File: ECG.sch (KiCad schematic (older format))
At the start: 16 parts, among them P1 MountingHole_Pad, P2 MountingHole_Pad, P3 MountingHole_Pad, U1 ADR4525, U2 SP6641

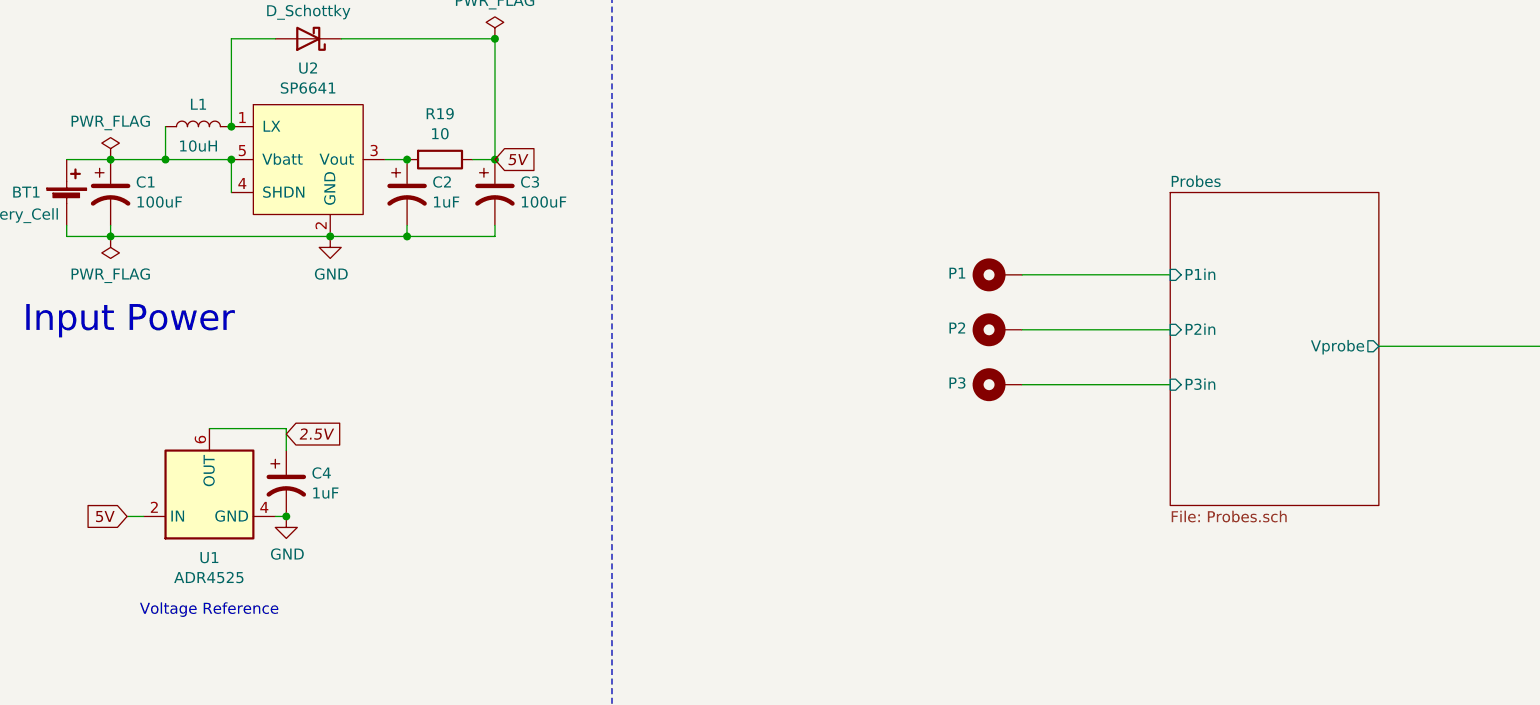
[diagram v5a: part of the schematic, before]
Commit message: #2 - Add ECG input via headphone jack
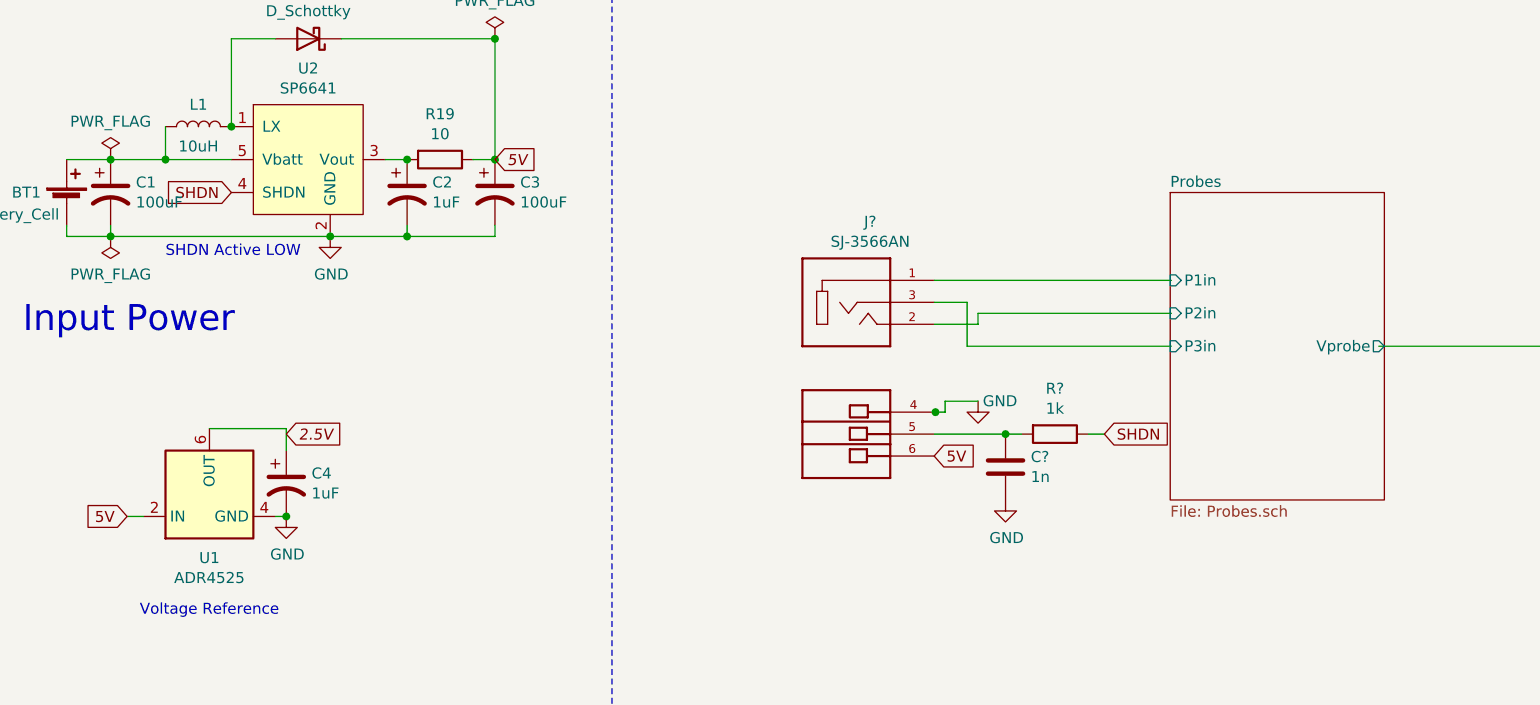
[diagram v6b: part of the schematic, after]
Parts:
- removed P1, P2, P3: MountingHole_Pad, MountingHole:MountingHole_6mm_Pad_Via, symbol Mechanical:MountingHole_Pad
- added C?: 1n, Capacitor_SMD:C_0805_2012Metric_Pad1.18x1.45mm_HandSolder, symbol Device:C
- added J?: SJ-3566AN, CUI_SJ-3566AN, symbol Audio_Connectors:SJ-3566AN
- added R?: 1k, Resistor_SMD:R_0805_2012Metric_Pad1.20x1.40mm_HandSolder, symbol Device:R
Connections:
- net labels added: SHDN
- wire segments 28 -> 38
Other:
- note added: "SHDN Active LOW\n"
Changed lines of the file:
@@
 Connection ~ 2400 4275
 $Sheet
-S 6425 2800 950  1425
+S 6425 2800 975  1400
 U 5F9F8A5A
 F0 "Probes" 50
 F1 "Probes.sch" 50
-F2 "Vprobe" O R 7375 3500 50
-F3 "P1in" I L 6425 3175 50
-F4 "P2in" I L 6425 3425 50
-F5 "P3in" I L 6425 3675 50
+F2 "Vprobe" O R 7400 3500 50
+F3 "P1in" I L 6425 3200 50
+F4 "P2in" I L 6425 3350 50
+F5 "P3in" I L 6425 3500 50
 $EndSheet
 $Sheet
@@
 Wire Wire Line
 	7375 3500 8375 3500
-$Comp
-L Mechanical:MountingHole_Pad P1
-U 1 1 5FA67DA7
-P 5650 3175
-F 0 "P1" V 5656 3327 50  0000 L CNN
-F 1 "MountingHole_Pad" V 5750 3133 50  0001 L CNN
-F 2 "MountingHole:MountingHole_6mm_Pad_Via" H 5650 3175 50  0001 C CNN
-F 3 "~" H 5650 3175 50  0001 C CNN
-	1    5650 3175
-	0    -1   -1   0
-$EndComp
-$Comp
-L Mechanical:MountingHole_Pad P2
-U 1 1 5FA685AE
-P 5650 3425
-F 0 "P2" V 5656 3577 50  0000 L CNN
-F 1 "MountingHole_Pad" V 5750 3383 50  0001 L CNN
-F 2 "MountingHole:MountingHole_6mm_Pad_Via" H 5650 3425 50  0001 C CNN
-F 3 "~" H 5650 3425 50  0001 C CNN
-	1    5650 3425
-	0    -1   -1   0
-$EndComp
-$Comp
-L Mechanical:MountingHole_Pad P3
-U 1 1 5FA686F5
-P 5650 3675
-F 0 "P3" V 5656 3827 50  0000 L CNN
-F 1 "MountingHole_Pad" V 5750 3633 50  0001 L CNN
-F 2 "MountingHole:MountingHole_6mm_Pad_Via" H 5650 3675 50  0001 C CNN
-F 3 "~" H 5650 3675 50  0001 C CNN
-	1    5650 3675
-	0    -1   -1   0
-$EndComp
-Wire Wire Line
-	5750 3175 6425 3175
-Wire Wire Line
-	5750 3425 6425 3425
-Wire Wire Line
-	6425 3675 5750 3675
 Wire Wire Line
 	10250 3500 9450 3500
@@
 $EndComp
 Wire Wire Line
-	2150 2650 2150 2800
-Connection ~ 2150 2650
-Wire Wire Line
 	1400 2650 1600 2650
 $Comp
@@
 $EndComp
 Connection ~ 3350 2100
+Text GLabel 2150 2800 0    50   Input ~ 0
+SHDN
+Text GLabel 6125 3900 2    50   Input ~ 0
+SHDN
+$Comp
+L Device:R R?
+U 1 1 5FBC4C0E
+P 5900 3900
+F 0 "R?" V 5693 3900 50  0000 C CNN
+F 1 "1k" V 5784 3900 50  0000 C CNN
+F 2 "Resistor_SMD:R_0805_2012Metric_Pad1.20x1.40mm_HandSolder" V 5830 3900 50  0001 C CNN
+F 3 "~" H 5900 3900 50  0001 C CNN
+	1    5900 3900
+	0    1    1    0
+$EndComp
+Wire Wire Line
+	6125 3900 6050 3900
+Text GLabel 5350 4000 2    50   Input ~ 0
+5V
+$Comp
+L power:GND #PWR?
+U 1 1 5FBD650D
+P 5550 3750
+F 0 "#PWR?" H 5550 3500 50  0001 C CNN
+F 1 "GND" H 5650 3750 50  0000 C CNN
+F 2 "" H 5550 3750 50  0001 C CNN
+F 3 "" H 5550 3750 50  0001 C CNN
+	1    5550 3750
+	1    0    0    -1
+$EndComp
+$Comp
+L power:GND #PWR?
+U 1 1 5FBD4F8F
+P 5675 4200
+F 0 "#PWR?" H 5675 3950 50  0001 C CNN
+F 1 "GND" H 5680 4027 50  0000 C CNN
+F 2 "" H 5675 4200 50  0001 C CNN
+F 3 "" H 5675 4200 50  0001 C CNN
+	1    5675 4200
+	1    0    0    -1
+$EndComp
+Connection ~ 5675 3900
+Wire Wire Line
+	5750 3900 5675 3900
+Wire Wire Line
+	5550 3350 6430 3350
+$Comp
+L Device:C C?
+U 1 1 5FBC41CD
+P 5675 4050
+F 0 "C?" H 5790 4096 50  0000 L CNN
+F 1 "1n" H 5790 4005 50  0000 L CNN
+F 2 "Capacitor_SMD:C_0805_2012Metric_Pad1.18x1.45mm_HandSolder" H 5713 3900 50  0001 C CNN
+F 3 "~" H 5675 4050 50  0001 C CNN
+	1    5675 4050
+	1    0    0    -1
+$EndComp
+$Comp
+L Audio_Connectors:SJ-3566AN J?
+U 1 1 5FBB1E3E
+P 4950 3300
+F 0 "J?" H 5059 3667 50  0000 C CNN
+F 1 "SJ-3566AN" H 5059 3576 50  0000 C CNN
+F 2 "CUI_SJ-3566AN" H 4950 3300 50  0001 L BNN
+F 3 "" H 4950 3300 50  0001 L BNN
+F 4 "Manufacturer recommendations" H 4950 3300 50  0001 L BNN "STANDARD"
+F 5 "" H 4950 3300 50  0001 L BNN "PARTREV"
+F 6 "CUI Inc" H 4950 3300 50  0001 L BNN "MF"
+	1    4950 3300
+	1    0    0    -1
+$EndComp
+Wire Wire Line
+	5550 3350 5550 3400
+Wire Wire Line
+	5500 3500 5500 3300
+Wire Wire Line
+	5500 3500 6430 3500
+Wire Wire Line
+	5400 3800 5400 3750
+Wire Wire Line
+	5400 3750 5550 3750
+Wire Wire Line
+	5350 3800 5356 3800
+Connection ~ 5356 3800
+Wire Wire Line
+	5356 3800 5400 3800
+Wire Wire Line
+	5350 3900 5675 3900
+Wire Wire Line
+	5350 3300 5500 3300
+Wire Wire Line
+	5350 3400 5550 3400
+Wire Wire Line
+	5350 3200 6430 3200
+Text Notes 1850 3100 0    50   ~ 0
+SHDN Active LOW\n
 $EndSCHEMATC

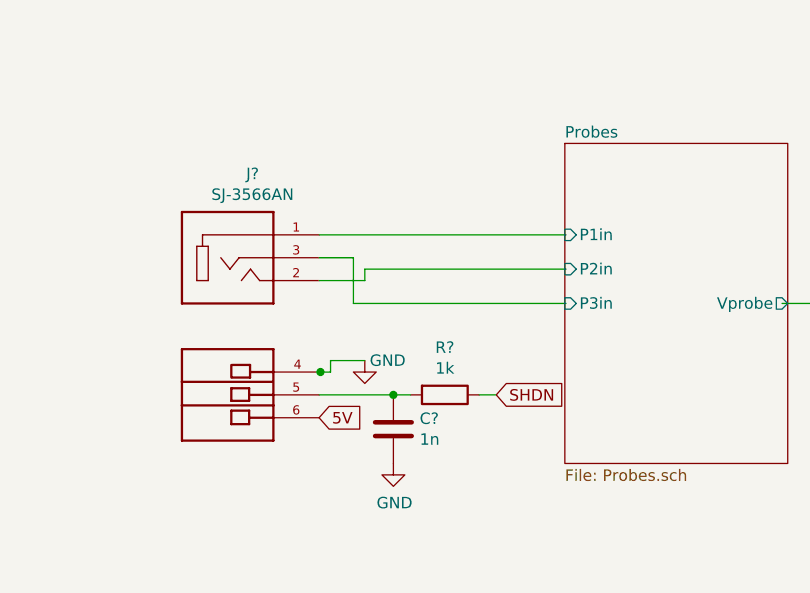
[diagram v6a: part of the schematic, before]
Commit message: #2 - Add ECG input via headphone jack
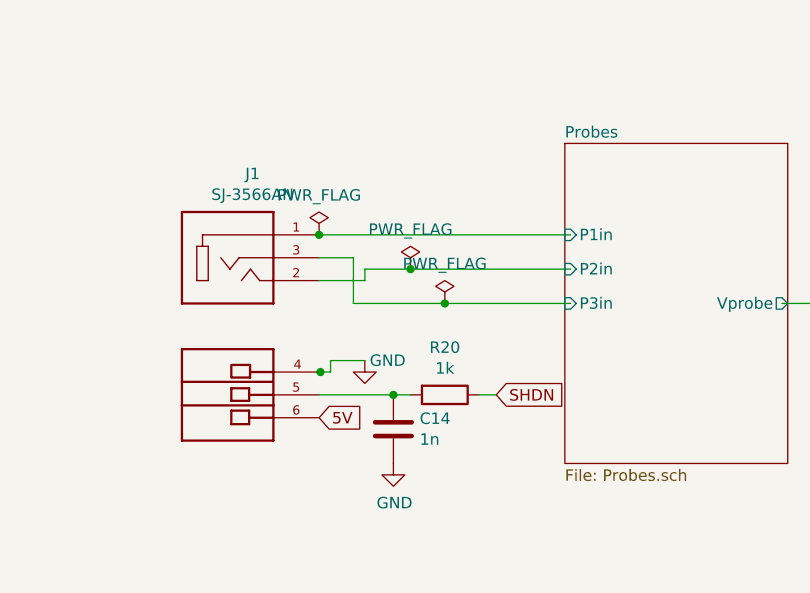
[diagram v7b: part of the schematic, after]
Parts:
- gave numbers to parts that had none: 3
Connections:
- wire segments 38 -> 40
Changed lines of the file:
@@
 SHDN
 $Comp
-L Device:R R?
+L Device:R R20
 U 1 1 5FBC4C0E
 P 5900 3900
-F 0 "R?" V 5693 3900 50  0000 C CNN
+F 0 "R20" V 5693 3900 50  0000 C CNN
 F 1 "1k" V 5784 3900 50  0000 C CNN
 F 2 "Resistor_SMD:R_0805_2012Metric_Pad1.20x1.40mm_HandSolder" V 5830 3900 50  0001 C CNN
@@
 5V
 $Comp
-L power:GND #PWR?
+L power:GND #PWR011
 U 1 1 5FBD650D
 P 5550 3750
-F 0 "#PWR?" H 5550 3500 50  0001 C CNN
+F 0 "#PWR011" H 5550 3500 50  0001 C CNN
 F 1 "GND" H 5650 3750 50  0000 C CNN
 F 2 "" H 5550 3750 50  0001 C CNN
@@
 $EndComp
 $Comp
-L power:GND #PWR?
+L power:GND #PWR012
 U 1 1 5FBD4F8F
 P 5675 4200
-F 0 "#PWR?" H 5675 3950 50  0001 C CNN
+F 0 "#PWR012" H 5675 3950 50  0001 C CNN
 F 1 "GND" H 5680 4027 50  0000 C CNN
 F 2 "" H 5675 4200 50  0001 C CNN
@@
 Wire Wire Line
 	5750 3900 5675 3900
-Wire Wire Line
-	5550 3350 6430 3350
 $Comp
-L Device:C C?
+L Device:C C14
 U 1 1 5FBC41CD
 P 5675 4050
-F 0 "C?" H 5790 4096 50  0000 L CNN
+F 0 "C14" H 5790 4096 50  0000 L CNN
 F 1 "1n" H 5790 4005 50  0000 L CNN
 F 2 "Capacitor_SMD:C_0805_2012Metric_Pad1.18x1.45mm_HandSolder" H 5713 3900 50  0001 C CNN
@@
 $EndComp
 $Comp
-L Audio_Connectors:SJ-3566AN J?
+L Audio_Connectors:SJ-3566AN J1
 U 1 1 5FBB1E3E
 P 4950 3300
-F 0 "J?" H 5059 3667 50  0000 C CNN
+F 0 "J1" H 5059 3667 50  0000 C CNN
 F 1 "SJ-3566AN" H 5059 3576 50  0000 C CNN
 F 2 "CUI_SJ-3566AN" H 4950 3300 50  0001 L BNN
@@
 Wire Wire Line
 	5500 3500 5500 3300
-Wire Wire Line
-	5500 3500 6430 3500
 Wire Wire Line
 	5400 3800 5400 3750
@@
 Wire Wire Line
 	5350 3400 5550 3400
-Wire Wire Line
-	5350 3200 6430 3200
 Text Notes 1850 3100 0    50   ~ 0
 SHDN Active LOW\n
+Wire Wire Line
+	5550 3350 5750 3350
+Wire Wire Line
+	5500 3500 5900 3500
+Wire Wire Line
+	6450 3200 5350 3200
+$Comp
+L power:PWR_FLAG #FLG0104
+U 1 1 5FBE011F
+P 5350 3200
+F 0 "#FLG0104" H 5350 3275 50  0001 C CNN
+F 1 "PWR_FLAG" H 5350 3373 50  0000 C CNN
+F 2 "" H 5350 3200 50  0001 C CNN
+F 3 "~" H 5350 3200 50  0001 C CNN
+	1    5350 3200
+	1    0    0    -1
+$EndComp
+Connection ~ 5350 3200
+$Comp
+L power:PWR_FLAG #FLG01
+U 1 1 5FBE0B2C
+P 5750 3350
+F 0 "#FLG01" H 5750 3425 50  0001 C CNN
+F 1 "PWR_FLAG" H 5750 3523 50  0000 C CNN
+F 2 "" H 5750 3350 50  0001 C CNN
+F 3 "~" H 5750 3350 50  0001 C CNN
+	1    5750 3350
+	1    0    0    -1
+$EndComp
+Connection ~ 5750 3350
+Wire Wire Line
+	5750 3350 6450 3350
+$Comp
+L power:PWR_FLAG #FLG02
+U 1 1 5FBE0E73
+P 5900 3500
+F 0 "#FLG02" H 5900 3575 50  0001 C CNN
+F 1 "PWR_FLAG" H 5900 3673 50  0000 C CNN
+F 2 "" H 5900 3500 50  0001 C CNN
+F 3 "~" H 5900 3500 50  0001 C CNN
+	1    5900 3500
+	1    0    0    -1
+$EndComp
+Connection ~ 5900 3500
+Wire Wire Line
+	5900 3500 6450 3500
 $EndSCHEMATC

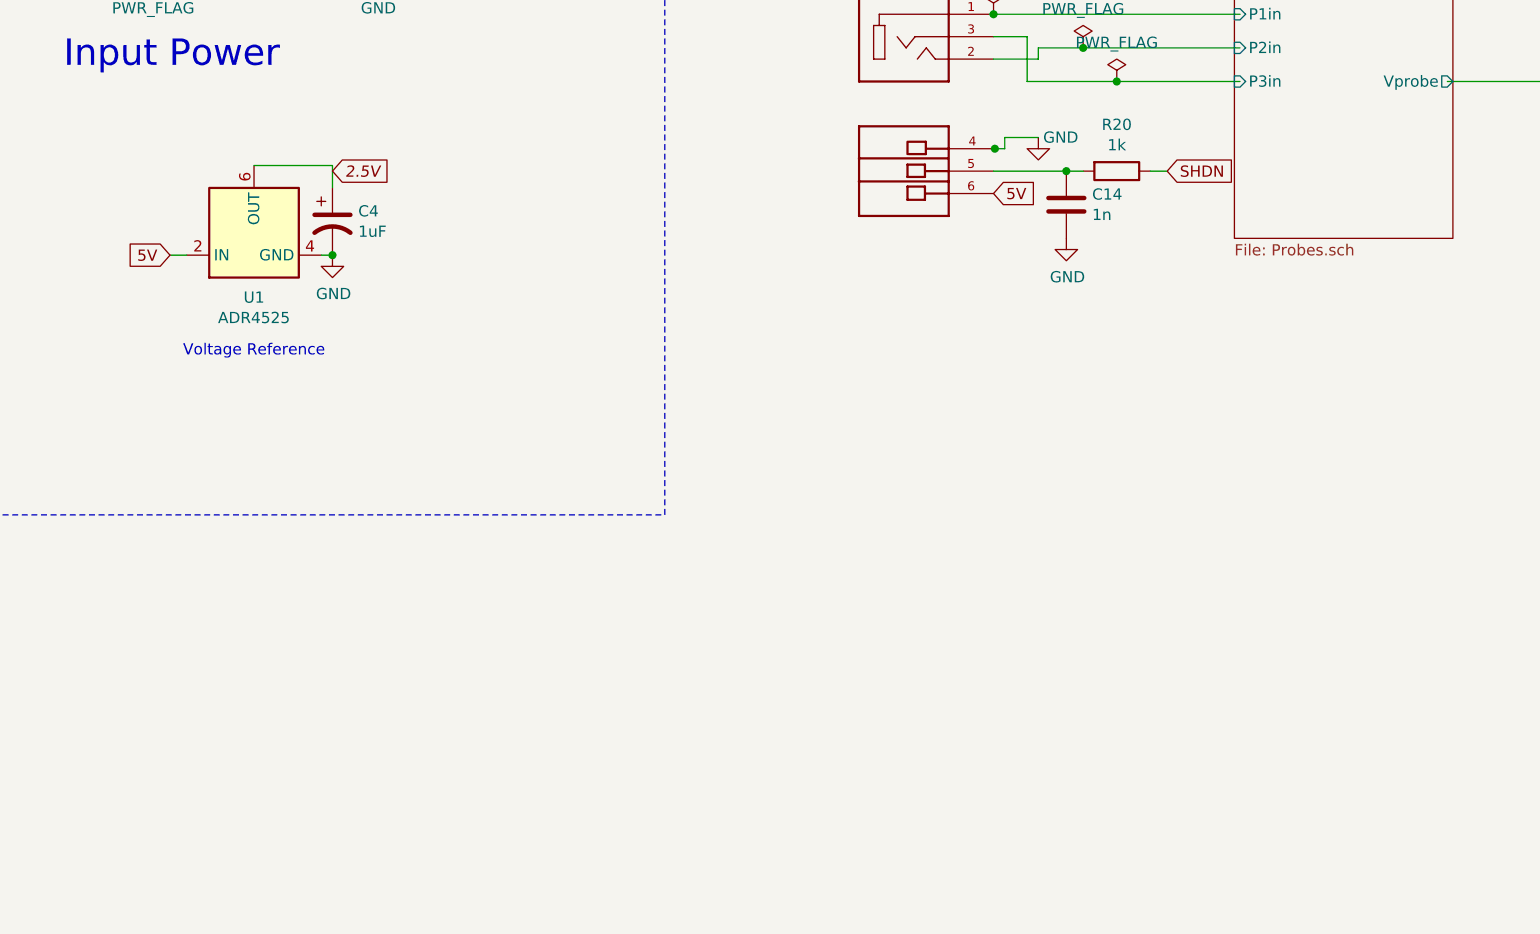
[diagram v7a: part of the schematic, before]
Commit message: #3 - Add power switch
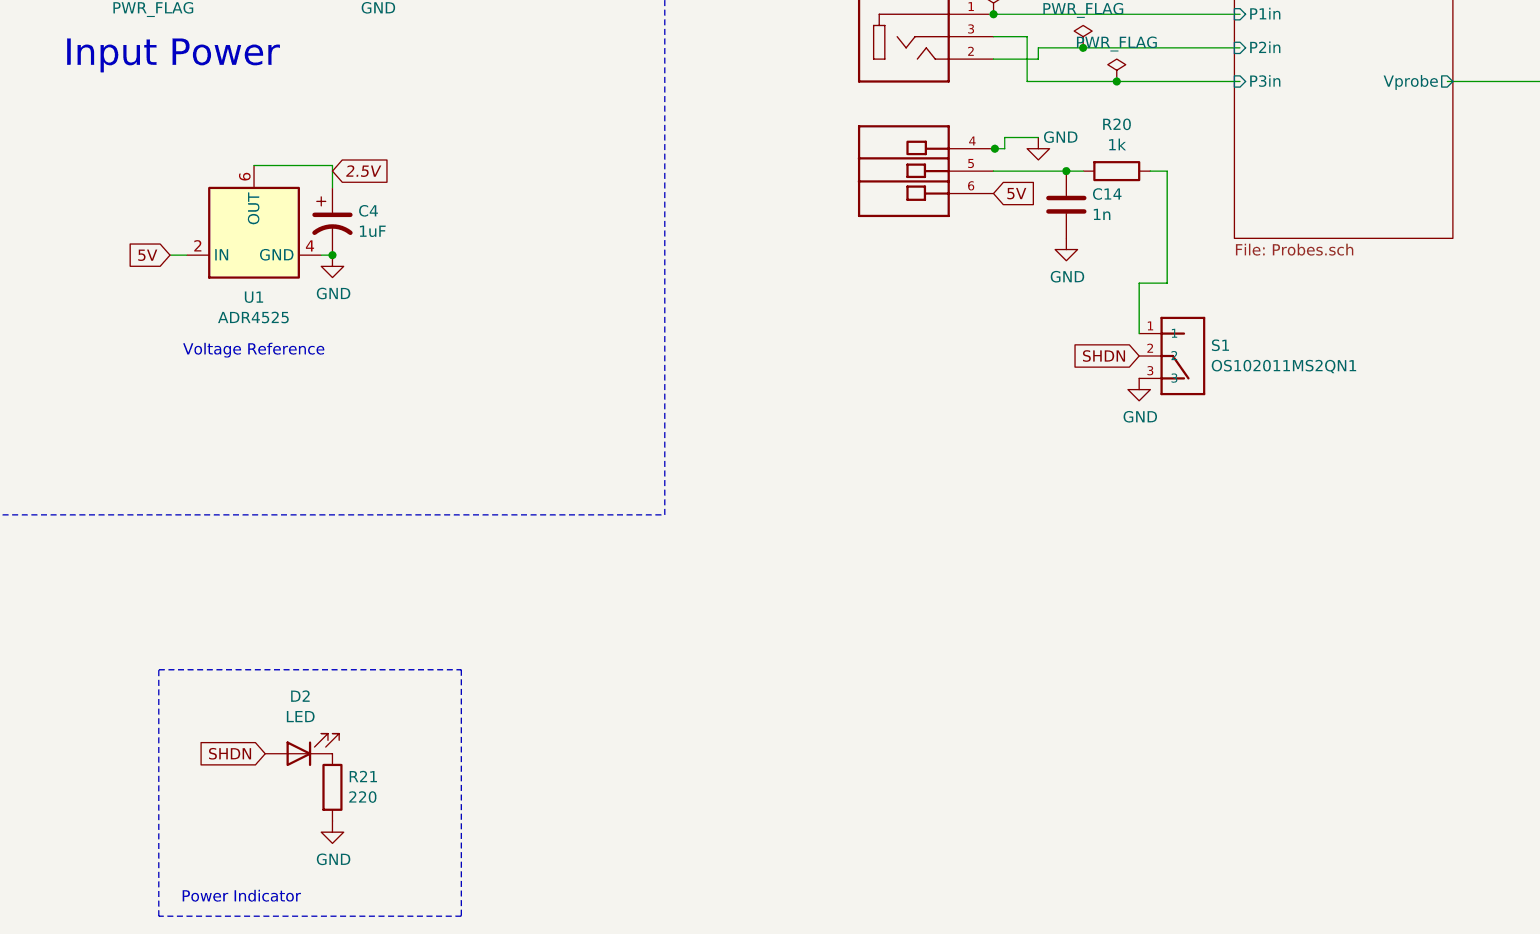
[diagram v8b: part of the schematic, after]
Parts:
- added D2: LED, Diode_SMD:D_0603_1608Metric_Pad1.05x0.95mm_HandSolder, symbol Device:LED
- added R21: 220, Resistor_SMD:R_0805_2012Metric_Pad1.20x1.40mm_HandSolder, symbol Device:R
- added S1: OS102011MS2QN1, SW_OS102011MS2QN1, symbol Switches:OS102011MS2QN1
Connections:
- wire segments 40 -> 43
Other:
- note added: "Power Indicator"
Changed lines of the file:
@@
 Text GLabel 2150 2800 0    50   Input ~ 0
 SHDN
-Text GLabel 6125 3900 2    50   Input ~ 0
+Text GLabel 6000 4725 0    50   Input ~ 0
 SHDN
 $Comp
@@
 Wire Wire Line
 	5900 3500 6450 3500
+$Comp
+L Switches:OS102011MS2QN1 S1
+U 1 1 5FBC1FC8
+P 6200 4725
+F 0 "S1" H 6320 4771 50  0000 L CNN
+F 1 "OS102011MS2QN1" H 6320 4680 50  0000 L CNN
+F 2 "SW_OS102011MS2QN1" H 6200 4725 50  0001 L BNN
+F 3 "" H 6200 4725 50  0001 L BNN
+F 4 "C&K" H 6200 4725 50  0001 L BNN "MANUFACTURER"
+F 5 "MANUFACTURER RECOMMENDATIONS" H 6200 4725 50  0001 L BNN "STANDARD"
+	1    6200 4725
+	1    0    0    -1
+$EndComp
+Wire Wire Line
+	6125 3900 6125 4400
+Wire Wire Line
+	6125 4400 6000 4400
+Wire Wire Line
+	6000 4400 6000 4625
+$Comp
+L power:GND #PWR014
+U 1 1 5FBCC4F0
+P 6000 4825
+F 0 "#PWR014" H 6000 4575 50  0001 C CNN
+F 1 "GND" H 6005 4652 50  0000 C CNN
+F 2 "" H 6000 4825 50  0001 C CNN
+F 3 "" H 6000 4825 50  0001 C CNN
+	1    6000 4825
+	1    0    0    -1
+$EndComp
+$Comp
+L Device:R R21
+U 1 1 5FBCD069
+P 2400 6650
+F 0 "R21" H 2470 6696 50  0000 L CNN
+F 1 "220" H 2470 6605 50  0000 L CNN
+F 2 "Resistor_SMD:R_0805_2012Metric_Pad1.20x1.40mm_HandSolder" V 2330 6650 50  0001 C CNN
+F 3 "~" H 2400 6650 50  0001 C CNN
+	1    2400 6650
+	1    0    0    -1
+$EndComp
+$Comp
+L power:GND #PWR013
+U 1 1 5FBD0E7E
+P 2400 6800
+F 0 "#PWR013" H 2400 6550 50  0001 C CNN
+F 1 "GND" H 2405 6627 50  0000 C CNN
+F 2 "" H 2400 6800 50  0001 C CNN
+F 3 "" H 2400 6800 50  0001 C CNN
+	1    2400 6800
+	1    0    0    -1
+$EndComp
+Text GLabel 2100 6500 0    50   Input ~ 0
+SHDN
+$Comp
+L Device:LED D2
+U 1 1 5FBD2826
+P 2250 6500
+F 0 "D2" H 2243 6245 50  0000 C CNN
+F 1 "LED" H 2243 6336 50  0000 C CNN
+F 2 "Diode_SMD:D_0603_1608Metric_Pad1.05x0.95mm_HandSolder" H 2250 6500 50  0001 C CNN
+F 3 "~" H 2250 6500 50  0001 C CNN
+	1    2250 6500
+	-1   0    0    1
+$EndComp
+Wire Notes Line
+	2975 6125 2975 7225
+Wire Notes Line
+	2975 7225 1625 7225
+Wire Notes Line
+	1625 7225 1625 6125
+Wire Notes Line
+	1625 6125 2975 6125
+Text Notes 1725 7175 0    50   ~ 0
+Power Indicator
 $EndSCHEMATC
